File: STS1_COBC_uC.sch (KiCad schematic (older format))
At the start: 39 parts, among them IC1 STM32F411RET6TR, IC2 STWD100PYW83F, J12 Conn_01x03_Male, J3 Conn_ARM_JTAG_SWD_10, J30 Conn_01x01_Male, J31 Conn_01x01_Male, J4 Conn_01x01_Male, J41 Conn_01x01_Male, J44 Conn_01x01_Male, J45 Conn_01x01_Male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

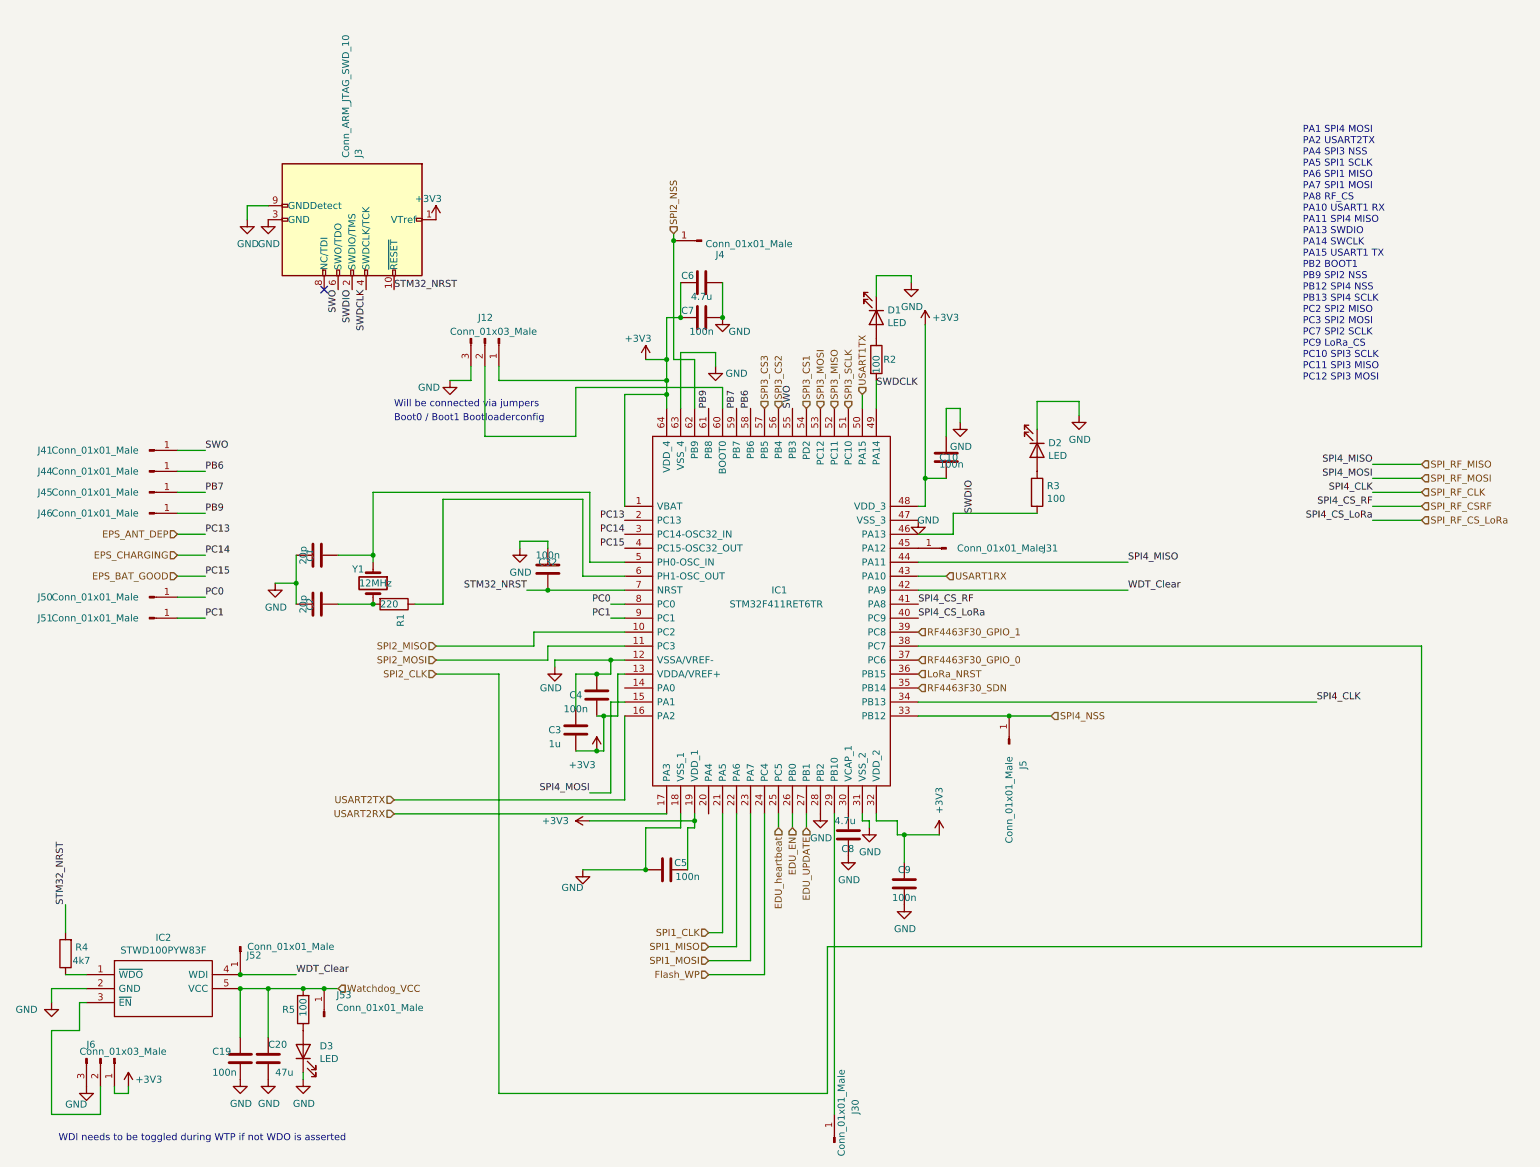
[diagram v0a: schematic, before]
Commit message: added powerplane + testpoints + some debugging
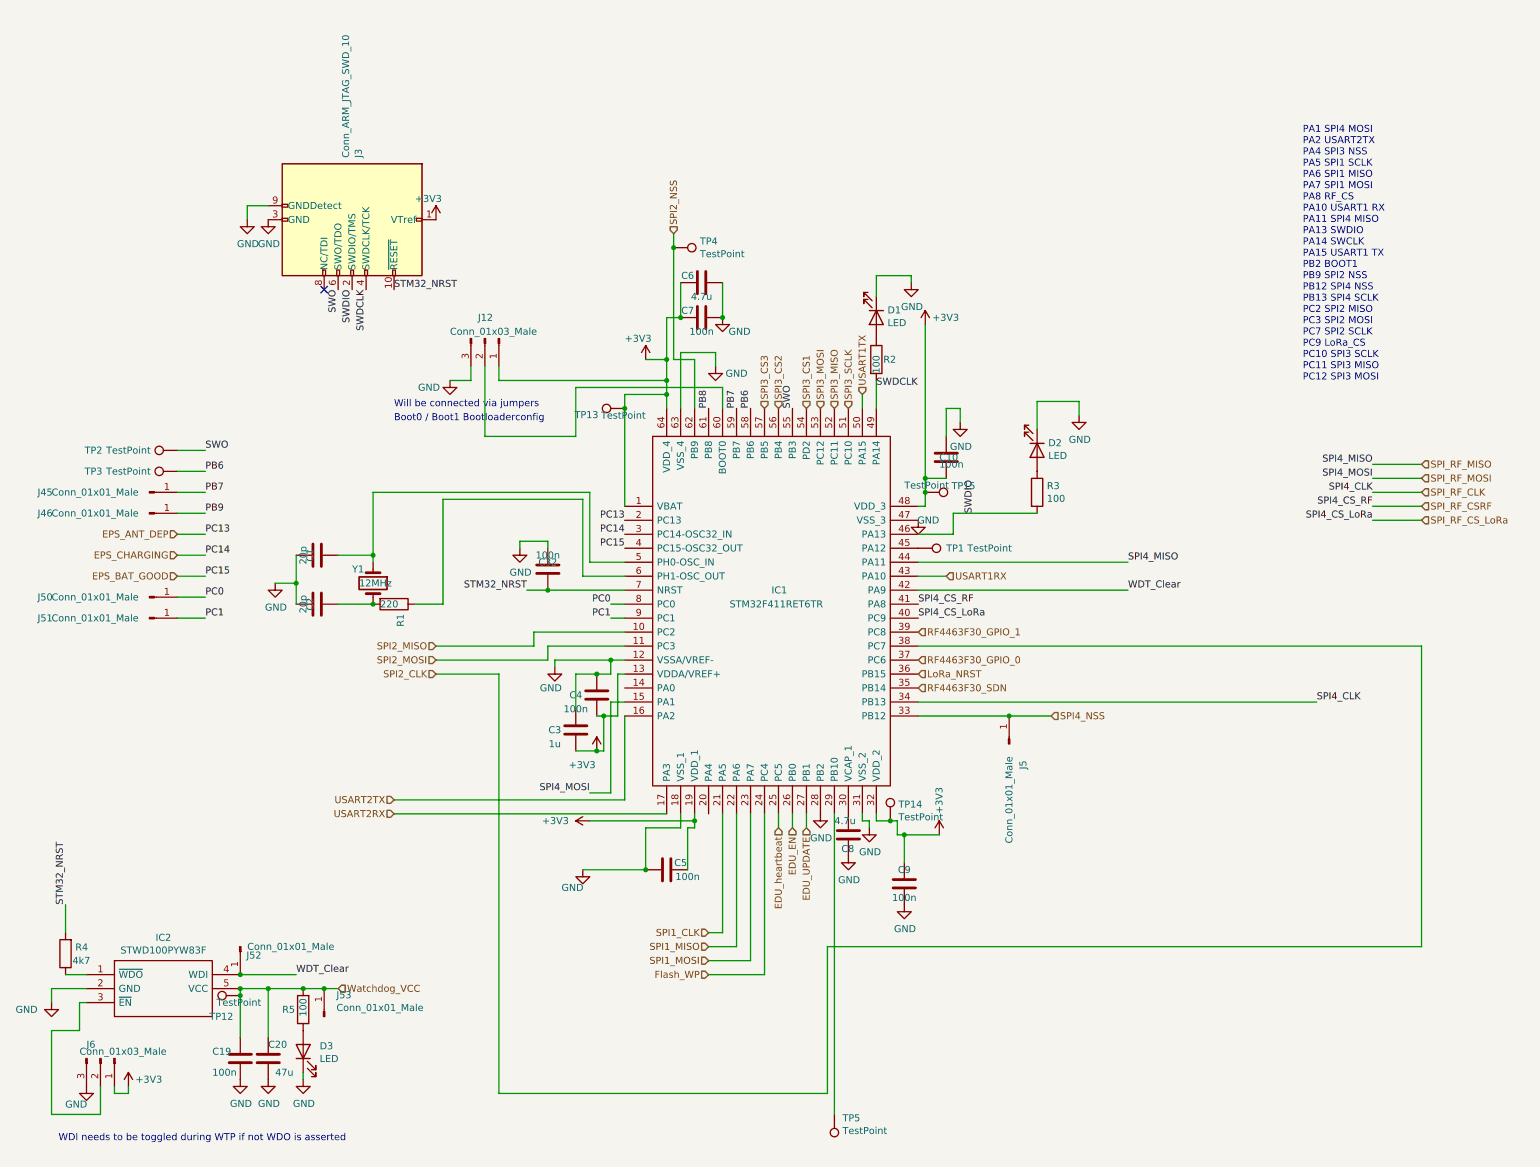
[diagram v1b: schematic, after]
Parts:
- removed J30, J31, J4, J41, J44: Conn_01x01_Male, Connector_PinHeader_2.54mm:PinHeader_1x01_P2.54mm_Vertical, symbol Connector:Conn_01x01_Male
- added TP1, TP12, TP13, TP14, TP15, TP2, TP3, TP4, TP5: TestPoint, STS1library:STS1_Testpoint, symbol Connector:TestPoint
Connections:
- net +3V3: now also TP13.1, TP14.1, TP15.1
- net PB6: now also TP3.1
- net PB9: no longer IC1.61 (PB8)
- net SPI2_NSS: now also TP4.1
- net SWO: now also TP2.1
- net Watchdog_VCC: now also TP12.1
- net at IC1.29 (PB10): now also TP5.1
- net at IC1.45 (PA12): now also TP1.1
- new net PB8: IC1.61 (PB8)
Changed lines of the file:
@@
 	6900 3650 8400 3650
 Wire Wire Line
-	6600 5300 6750 5300
+	6600 5300 6700 5300
 Wire Wire Line
 	5150 2000 5300 2000
@@
 Wire Wire Line
 	5800 6400 5800 5250
-$Comp
-L Connector:Conn_01x01_Male J31
-U 1 1 616CBBC3
-P 7100 3350
-F 0 "J31" H 6300 3350 50  0000 L CNN
-F 1 "Conn_01x01_Male" H 6400 3350 50  0000 L CNN
-F 2 "Connector_PinHeader_2.54mm:PinHeader_1x01_P2.54mm_Vertical" H 7100 3350 50  0001 C CNN
-F 3 "~" H 7100 3350 50  0001 C CNN
-	1    7100 3350
-	-1   0    0    1
-$EndComp
 Wire Wire Line
 	10500 4050 10500 6200
@@
 Wire Wire Line
 	6250 6200 10500 6200
-$Comp
-L Connector:Conn_01x01_Male J30
-U 1 1 61702BE6
-P 6300 7600
-F 0 "J30" H 6500 7450 50  0000 L CNN
-F 1 "Conn_01x01_Male" H 6200 7550 50  0000 L CNN
-F 2 "Connector_PinHeader_2.54mm:PinHeader_1x01_P2.54mm_Vertical" H 6300 7600 50  0001 C CNN
-F 3 "~" H 6300 7600 50  0001 C CNN
-	1    6300 7600
-	0    -1   -1   0
-$EndComp
 Wire Wire Line
 	6300 7400 6300 5250
@@
 	4800 5150 4800 4550
 Wire Wire Line
-	6950 3050 6950 2850
+	6950 3050 6950 2950
 $Comp
 L Connector:Conn_01x01_Male J51
@@
 	1600 3550 1800 3550
 Text Label 5400 2350 1    50   ~ 0
-PB9
+PB8
 Text Label 5600 2350 1    50   ~ 0
 PB7
@@
 	1    0    0    -1
 $EndComp
-$Comp
-L Connector:Conn_01x01_Male J44
-U 1 1 6177F2AE
-P 1400 2800
-F 0 "J44" H 600 2800 50  0000 L CNN
-F 1 "Conn_01x01_Male" H 700 2800 50  0000 L CNN
-F 2 "Connector_PinHeader_2.54mm:PinHeader_1x01_P2.54mm_Vertical" H 1400 2800 50  0001 C CNN
-F 3 "~" H 1400 2800 50  0001 C CNN
-	1    1400 2800
-	1    0    0    -1
-$EndComp
 Text Label 1800 3100 0    50   ~ 0
 PB9
@@
 Wire Wire Line
 	1600 2800 1800 2800
-$Comp
-L Connector:Conn_01x01_Male J41
-U 1 1 617A65E0
-P 1400 2650
-F 0 "J41" H 600 2650 50  0000 L CNN
-F 1 "Conn_01x01_Male" H 700 2650 50  0000 L CNN
-F 2 "Connector_PinHeader_2.54mm:PinHeader_1x01_P2.54mm_Vertical" H 1400 2650 50  0001 C CNN
-F 3 "~" H 1400 2650 50  0001 C CNN
-	1    1400 2650
-	1    0    0    -1
-$EndComp
 Wire Wire Line
 	1600 2650 1800 2650
@@
 Connection ~ 2250 6500
 Wire Wire Line
-	2050 6500 2050 6850
+	2050 6500 2050 6550
 Connection ~ 2050 6500
 $Comp
@@
 	4250 4050 4800 4050
 Wire Wire Line
-	5150 1100 5150 1150
-Wire Wire Line
 	6900 4550 7550 4550
 $Comp
@@
 Wire Wire Line
 	7550 4550 7850 4550
-$Comp
-L Connector:Conn_01x01_Male J4
-U 1 1 6198D698
-P 5350 1150
-F 0 "J4" H 5250 1250 50  0000 R CNN
-F 1 "Conn_01x01_Male" H 5322 1173 50  0000 R CNN
-F 2 "Connector_PinHeader_2.54mm:PinHeader_1x01_P2.54mm_Vertical" H 5350 1150 50  0001 C CNN
-F 3 "~" H 5350 1150 50  0001 C CNN
-	1    5350 1150
-	-1   0    0    1
-$EndComp
-Connection ~ 5150 1150
-Wire Wire Line
-	5150 1150 5150 2000
 Wire Wire Line
 	6800 5400 7050 5400
@@
 	3900 2150 5100 2150
 Wire Wire Line
-	4800 3050 4800 2250
+	4800 3050 4800 2350
 $Comp
 L STM32F411RET6TR:STM32F411RET6TR IC1
@@
 Wire Wire Line
 	6900 4450 9750 4450
+$Comp
+L Connector:TestPoint TP1
+U 1 1 61BEB8B5
+P 6900 3350
+F 0 "TP1" V 6900 3550 50  0000 L CNN
+F 1 "TestPoint" V 6900 3700 50  0000 L CNN
+F 2 "STS1library:STS1_Testpoint" H 7100 3350 50  0001 C CNN
+F 3 "~" H 7100 3350 50  0001 C CNN
+	1    6900 3350
+	0    1    1    0
+$EndComp
+Wire Wire Line
+	5150 1100 5150 1200
+$Comp
+L Connector:TestPoint TP4
+U 1 1 61B32C23
+P 5150 1200
+F 0 "TP4" V 5104 1388 50  0000 L CNN
+F 1 "TestPoint" V 5195 1388 50  0000 L CNN
+F 2 "STS1library:STS1_Testpoint" H 5350 1200 50  0001 C CNN
+F 3 "~" H 5350 1200 50  0001 C CNN
+	1    5150 1200
+	0    1    1    0
+$EndComp
+Connection ~ 5150 1200
+Wire Wire Line
+	5150 1200 5150 2000
+$Comp
+L Connector:TestPoint TP5
+U 1 1 61B34C92
+P 6300 7400
+F 0 "TP5" H 6242 7426 50  0000 R CNN
+F 1 "TestPoint" H 6242 7517 50  0000 R CNN
+F 2 "STS1library:STS1_Testpoint" H 6500 7400 50  0001 C CNN
+F 3 "~" H 6500 7400 50  0001 C CNN
+	1    6300 7400
+	-1   0    0    1
+$EndComp
+$Comp
+L Connector:TestPoint TP3
+U 1 1 61B36800
+P 1600 2800
+F 0 "TP3" V 1600 3400 50  0000 C CNN
+F 1 "TestPoint" V 1600 3150 50  0000 C CNN
+F 2 "STS1library:STS1_Testpoint" H 1800 2800 50  0001 C CNN
+F 3 "~" H 1800 2800 50  0001 C CNN
+	1    1600 2800
+	0    -1   -1   0
+$EndComp
+$Comp
+L Connector:TestPoint TP2
+U 1 1 61B3896D
+P 1600 2650
+F 0 "TP2" V 1600 3250 50  0000 C CNN
+F 1 "TestPoint" V 1600 3000 50  0000 C CNN
+F 2 "STS1library:STS1_Testpoint" H 1800 2650 50  0001 C CNN
+F 3 "~" H 1800 2650 50  0001 C CNN
+	1    1600 2650
+	0    -1   -1   0
+$EndComp
+$Comp
+L Connector:TestPoint TP14
+U 1 1 61B6F646
+P 6700 5300
+F 0 "TP14" H 6758 5418 50  0000 L CNN
+F 1 "TestPoint" H 6758 5327 50  0000 L CNN
+F 2 "STS1library:STS1_Testpoint" H 6900 5300 50  0001 C CNN
+F 3 "~" H 6900 5300 50  0001 C CNN
+	1    6700 5300
+	1    0    0    -1
+$EndComp
+Connection ~ 6700 5300
+Wire Wire Line
+	6700 5300 6750 5300
+$Comp
+L Connector:TestPoint TP15
+U 1 1 61B70087
+P 6950 2950
+F 0 "TP15" V 6904 3138 50  0000 L CNN
+F 1 "TestPoint" V 6900 2800 50  0000 L CNN
+F 2 "STS1library:STS1_Testpoint" H 7150 2950 50  0001 C CNN
+F 3 "~" H 7150 2950 50  0001 C CNN
+	1    6950 2950
+	0    1    1    0
+$EndComp
+Connection ~ 6950 2950
+Wire Wire Line
+	6950 2950 6950 2850
+$Comp
+L Connector:TestPoint TP13
+U 1 1 61B70D95
+P 4800 2350
+F 0 "TP13" V 4754 2538 50  0000 L CNN
+F 1 "TestPoint" V 4750 2200 50  0000 L CNN
+F 2 "STS1library:STS1_Testpoint" H 5000 2350 50  0001 C CNN
+F 3 "~" H 5000 2350 50  0001 C CNN
+	1    4800 2350
+	0    -1   -1   0
+$EndComp
+Connection ~ 4800 2350
+Wire Wire Line
+	4800 2350 4800 2250
+$Comp
+L Connector:TestPoint TP12
+U 1 1 61B721D9
+P 2050 6550
+F 0 "TP12" V 1900 6600 50  0000 L CNN
+F 1 "TestPoint" V 2000 6400 50  0000 L CNN
+F 2 "STS1library:STS1_Testpoint" H 2250 6550 50  0001 C CNN
+F 3 "~" H 2250 6550 50  0001 C CNN
+	1    2050 6550
+	0    -1   -1   0
+$EndComp
+Connection ~ 2050 6550
+Wire Wire Line
+	2050 6550 2050 6850
 $EndSCHEMATC

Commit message: finished prototype
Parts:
- R2, R3, R5: value 100 -> 300
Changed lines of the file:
@@
 P 6600 2000
 F 0 "R2" H 6650 2000 50  0000 L CNN
-F 1 "100" V 6600 1900 50  0000 L CNN
+F 1 "300" V 6600 1900 50  0000 L CNN
 F 2 "Resistor_SMD:R_0805_2012Metric" V 6530 2000 50  0001 C CNN
 F 3 "~" H 6600 2000 50  0001 C CNN
@@
 P 7750 2950
 F 0 "R3" H 7820 2996 50  0000 L CNN
-F 1 "100" H 7820 2905 50  0000 L CNN
+F 1 "300" H 7820 2905 50  0000 L CNN
 F 2 "Resistor_SMD:R_0805_2012Metric" V 7680 2950 50  0001 C CNN
 F 3 "~" H 7750 2950 50  0001 C CNN
@@
 AR Path="/61272FBF/6167419D" Ref="R5"  Part="1"
 F 0 "R5" H 2650 6650 50  0000 R CNN
-F 1 "100" V 2500 6700 50  0000 R CNN
+F 1 "300" V 2500 6700 50  0000 R CNN
 F 2 "Resistor_SMD:R_0805_2012Metric" V 2430 6650 50  0001 C CNN
 F 3 "~" H 2500 6650 50  0001 C CNN
